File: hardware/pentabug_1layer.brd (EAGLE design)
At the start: 33 x 82.9 mm, 17 parts, among them IC1 ATMEGA88

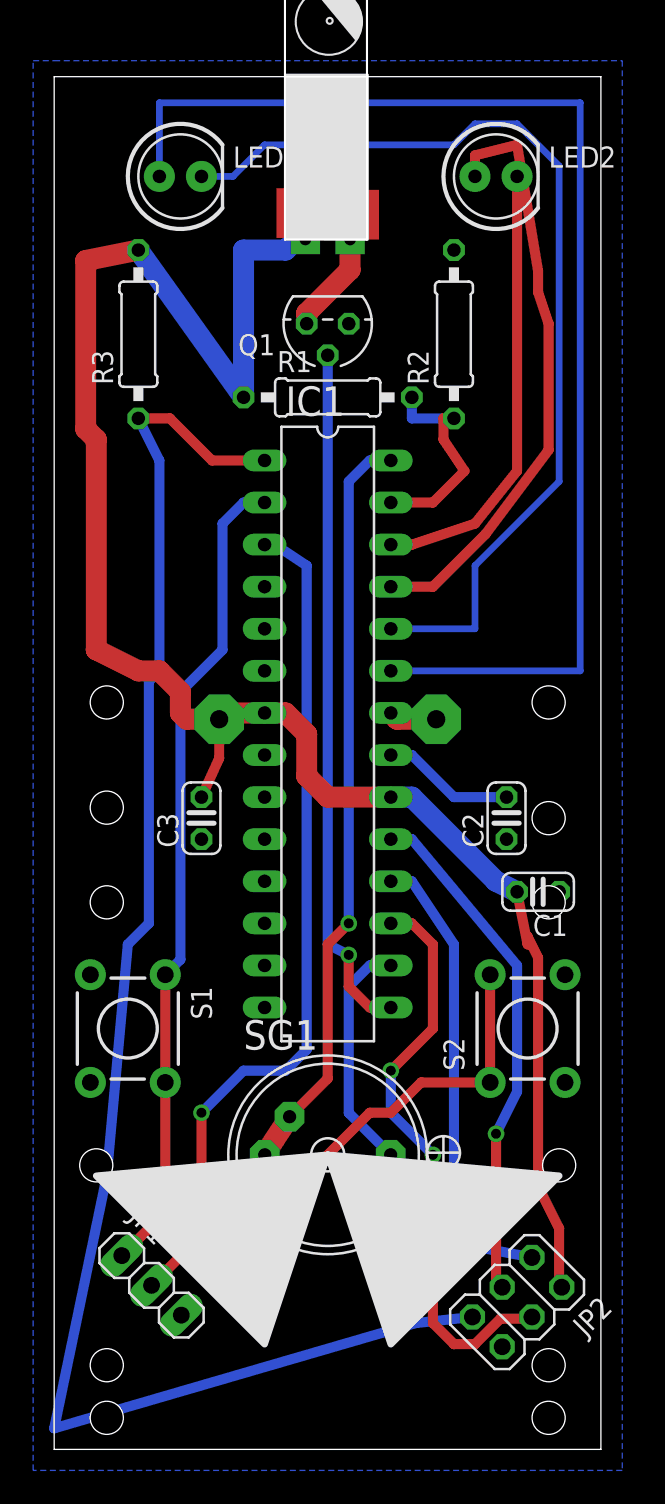
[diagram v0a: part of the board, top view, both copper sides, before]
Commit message: cleaned up and draw power lines
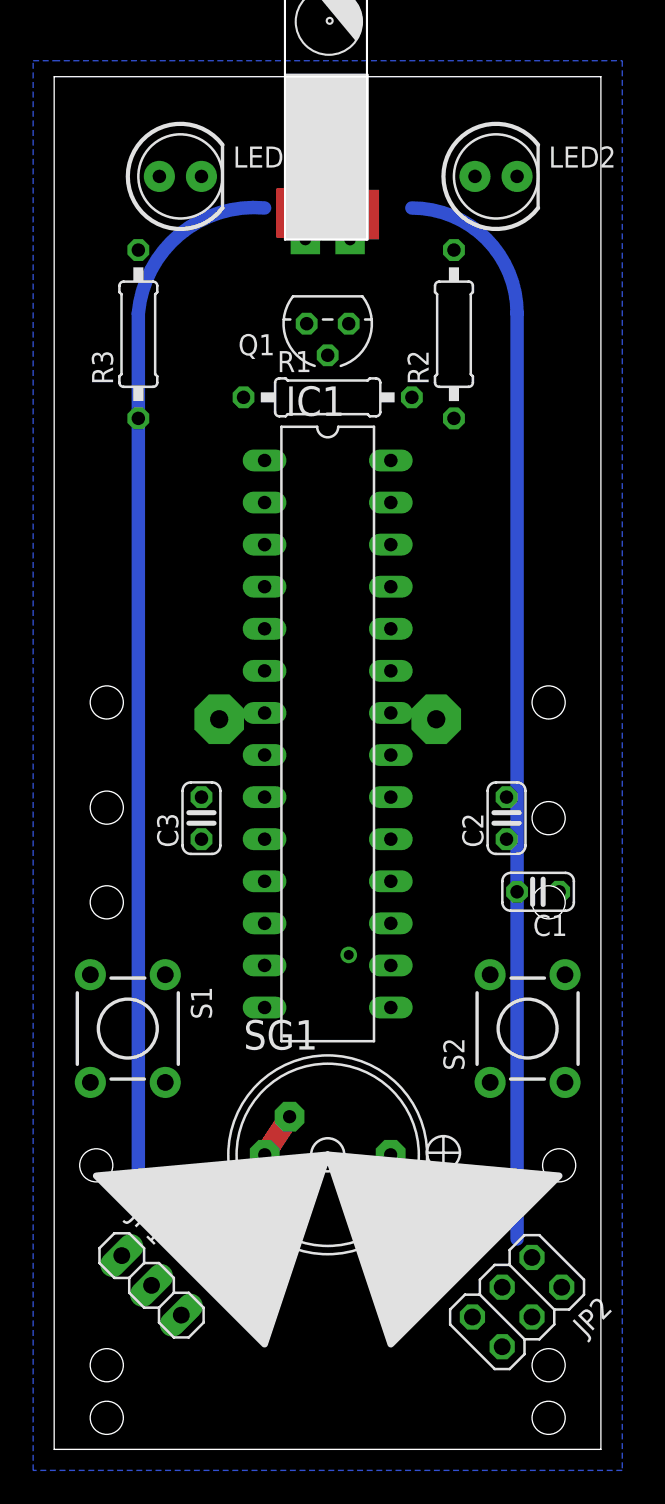
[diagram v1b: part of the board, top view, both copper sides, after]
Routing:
- net VCC: track 114.8 -> 0.00 mm
- net RST: track 97.3 -> 0.00 mm
- net TX: track 78.7 -> 0.00 mm, vias 1 -> 0
- net N$3: track 75.6 -> 0.00 mm
- net N$2: track 0.00 -> 64.9 mm
- net N$1: track 0.00 -> 63.3 mm
- net N$10: track 59.1 -> 0.00 mm
- net RX: track 49.8 -> 0.00 mm
- net BUZGND: track 42.9 -> 0.00 mm, vias 1 -> 0
- net VIBRATE: track 42.0 -> 0.00 mm
- net N$5: track 35.9 -> 0.00 mm
- net MOSI: track 35.2 -> 0.00 mm, vias 2 -> 0
- net SCK: track 31.1 -> 0.00 mm, vias 1 -> 0
- net MISO: track 28.6 -> 0.00 mm
- net BATTLVL: track 27.1 -> 0.00 mm
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
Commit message: made editable with eagle freeware!!
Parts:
- moved LED1 74.3 mm to (6.99, 8.89), turned to 90 degrees
- moved U$1 69.7 mm to (3.81, 17.8), turned to 180 degrees
- moved JP1 68.6 mm to (73.9, 7.15), turned to 45 degrees
- moved R3 68.3 mm to (16.5, 6.35), turned to 180 degrees
- moved S1 59.9 mm to (58.4, 5.71), turned to 0 degrees
- moved LED2 58.6 mm to (6.99, 27.9), turned to 90 degrees
- moved Q1 56.5 mm to (15.9, 17.8), turned to 270 degrees
- moved R1 52.2 mm to (20.3, 17.8), turned to 90 degrees
- moved C3 50.3 mm to (45.7, 10.2), turned to 180 degrees
- moved SG1 49.9 mm to (66.0, 17.8), turned to 90 degrees
- moved JP2 49.0 mm to (74.9, 29.2), turned to 315 degrees
- moved R2 48.9 mm to (16.5, 25.4), turned to 180 degrees
- moved BAT1 47.8 mm to (63.5, 17.8), turned to 180 degrees
- moved IC1 39.9 mm to (40.6, 17.8), turned to 0 degrees
- moved S2 29.9 mm to (58.4, 29.8), turned to 180 degrees
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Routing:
- net VCC: track 0.00 -> 137.0 mm
- net N$2: track 64.9 -> 0.00 mm
- net N$1: track 63.3 -> 0.00 mm
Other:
- board size 33 x 82.9 mm -> 82.9 x 33 mm

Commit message: inbetween
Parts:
- moved C1 5.08 mm to (50.2, 25.4)
- moved R3 3.59 mm to (19.1, 8.89)
- moved R2 2.84 mm to (19.1, 26.7)
- moved C2 2.01 mm to (45.1, 26.7)
- moved LED1 1.27 mm to (6.99, 7.62)
- moved C3 0.63 mm to (45.7, 9.53)
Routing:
- net RX: track 0.00 -> 48.5 mm
- net VCC: track 137.0 -> 184.7 mm
- net VIBRATE: track 0.00 -> 40.9 mm, vias 1 -> 0
- net TX: track 0.00 -> 38.7 mm, vias 0 -> 2
- net MOSI: track 0.00 -> 27.1 mm
- net MISO: track 0.00 -> 26.1 mm
- net RST: track 0.00 -> 23.9 mm
- net SCK: track 0.00 -> 17.5 mm
- net BATLVL: track 0.00 -> 13.9 mm
- net N$8: track 0.00 -> 5.97 mm
- net N$17: track 0.00 -> 5.72 mm
- net N$6: track 0.00 -> 0.64 mm

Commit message: inbetween
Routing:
- net BUZGND: track 0.00 -> 45.8 mm, vias 0 -> 2
- net TX: track 38.7 -> 71.9 mm, vias 2 -> 4
- net BUZZR: track 0.00 -> 13.0 mm
- net GND: track 0.00 -> 3.81 mm, vias 0 -> 2
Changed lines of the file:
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@@
 <grid distance="25" unitdist="mil" unit="mil" style="lines" multiple="2" display="yes" altdistance="10" altunitdist="mil" altunit="mil"/>
 <layers>
-<layer number="1" name="Top" color="4" fill="1" visible="no" active="yes"/>
+<layer number="1" name="Top" color="4" fill="1" visible="yes" active="yes"/>
 <layer number="2" name="Route2" color="1" fill="3" visible="no" active="no"/>
 <layer number="3" name="Route3" color="4" fill="3" visible="no" active="no"/>
@@
 <vertex x="85.09" y="0"/>
 </polygon>
-<wire x1="50.165" y1="26.67" x2="55.1688" y2="32.1056" width="0" layer="19" extent="1-1"/>
-<wire x1="41.91" y1="13.97" x2="39.37" y2="21.59" width="0" layer="19" extent="1-1"/>
+<via x="40.64" y="19.685" extent="1-16" drill="0.6" diameter="0.254" shape="octagon"/>
+<via x="40.64" y="15.875" extent="1-16" drill="0.6" diameter="0.254" shape="octagon"/>
+<wire x1="40.64" y1="19.685" x2="40.64" y2="15.875" width="0.4064" layer="1"/>
+<wire x1="46.355" y1="26.67" x2="39.75" y2="24.33" width="0" layer="19" extent="1-1"/>
+<wire x1="55.1688" y1="32.1056" x2="50.165" y2="26.67" width="0" layer="19" extent="1-1"/>
 <wire x1="55.1688" y1="3.4544" x2="46.99" y2="9.525" width="0" layer="19" extent="1-1"/>
+<wire x1="15.875" y1="19.05" x2="39.37" y2="21.59" width="0" layer="19" extent="1-1"/>
 </signal>
 <signal name="N$17">
@@
 <contactref element="JP1" pad="2"/>
 <contactref element="IC1" pad="3"/>
-<wire x1="60.96" y1="27.686" x2="55.88" y2="27.686" width="0.4064" layer="16"/>
+<wire x1="63.119" y1="27.686" x2="55.88" y2="27.686" width="0.4064" layer="16"/>
 <wire x1="55.626" y1="27.686" x2="33.401" y2="27.686" width="0.4064" layer="16"/>
 <wire x1="33.401" y1="27.686" x2="30.48" y2="24.765" width="0.4064" layer="16"/>
@@
 <wire x1="30.48" y1="15.748" x2="29.21" y2="13.97" width="0.4064" layer="16"/>
 <via x="30.48" y="19.685" extent="1-16" drill="0.6" diameter="0.254" shape="octagon"/>
-<wire x1="60.96" y1="27.686" x2="61.6712" y2="27.5844" width="0" layer="19" extent="16-16"/>
+<wire x1="30.48" y1="19.685" x2="30.48" y2="15.875" width="0.4064" layer="1"/>
+<via x="60.325" y="22.225" extent="1-16" drill="0.6" diameter="0.254" shape="octagon"/>
+<wire x1="60.325" y1="22.225" x2="73.914" y2="8.636" width="0.4064" layer="16"/>
+<wire x1="73.914" y1="8.636" x2="73.914" y2="7.112" width="0.4064" layer="16"/>
+<wire x1="63.5" y1="27.305" x2="60.325" y2="22.225" width="0.4064" layer="1"/>
+<wire x1="63.119" y1="27.686" x2="63.5" y2="27.305" width="0.4064" layer="16"/>
+<via x="63.5" y="27.432" extent="1-16" drill="0.6" diameter="0.254" shape="octagon"/>
+<wire x1="63.5" y1="27.305" x2="63.5" y2="27.432" width="0" layer="19" extent="16-16"/>
+<wire x1="63.5" y1="27.305" x2="63.5" y2="27.305" width="0" layer="19" extent="1-16"/>
+<wire x1="73.92" y1="7.147" x2="73.914" y2="7.112" width="0" layer="19" extent="16-16"/>
 <wire x1="55.626" y1="27.686" x2="55.88" y2="27.686" width="0" layer="19" extent="16-16"/>
+<wire x1="30.48" y1="15.748" x2="30.48" y2="15.875" width="0" layer="19" extent="1-1"/>
 <wire x1="55.1688" y1="27.5844" x2="55.626" y2="27.686" width="0" layer="19" extent="16-16"/>
-<wire x1="30.48" y1="15.748" x2="30.48" y2="19.685" width="0" layer="19" extent="16-16"/>
-<wire x1="73.92" y1="7.147" x2="61.6712" y2="27.5844" width="0" layer="19" extent="1-1"/>
+<wire x1="61.6712" y1="27.5844" x2="63.119" y2="27.686" width="0" layer="19" extent="16-16"/>
 </signal>
 <signal name="RX">
@@
 <contactref element="SG1" pad="+1"/>
 <contactref element="SG1" pad="+"/>
+<wire x1="66.04" y1="21.59" x2="64.135" y2="23.495" width="0.4064" layer="16"/>
+<wire x1="64.135" y1="23.495" x2="56.515" y2="23.495" width="0.4064" layer="16"/>
+<wire x1="56.515" y1="23.495" x2="54.61" y2="21.59" width="0.4064" layer="16"/>
 <wire x1="66.04" y1="21.59" x2="66.04" y2="21.58" width="0" layer="19" extent="1-1"/>
-<wire x1="54.61" y1="21.59" x2="66.04" y2="21.58" width="0" layer="19" extent="1-1"/>
+<wire x1="66.04" y1="21.59" x2="66.04" y2="21.59" width="0" layer="19" extent="1-16"/>
 </signal>
 <signal name="VIBRATE">
@@
 <contactref element="SG1" pad="-1"/>
 <contactref element="SG1" pad="-"/>
+<wire x1="63.754" y1="15.494" x2="63.373" y2="15.875" width="0.4064" layer="16"/>
+<wire x1="63.373" y1="15.875" x2="42.545" y2="15.875" width="0.4064" layer="16"/>
+<via x="42.545" y="15.875" extent="1-16" drill="0.6" diameter="0.254" shape="octagon"/>
+<wire x1="24.13" y1="21.59" x2="27.305" y2="18.415" width="0.4064" layer="16"/>
+<wire x1="27.305" y1="18.415" x2="41.91" y2="18.415" width="0.4064" layer="16"/>
+<via x="42.545" y="19.685" extent="1-16" drill="0.6" diameter="0.254" shape="octagon"/>
+<wire x1="41.91" y1="18.415" x2="42.545" y2="19.05" width="0.4064" layer="16"/>
+<wire x1="42.545" y1="19.05" x2="42.545" y2="19.685" width="0.4064" layer="16"/>
+<wire x1="42.545" y1="19.685" x2="42.545" y2="15.875" width="0.4064" layer="1"/>
 <wire x1="66.04" y1="13.98" x2="66.04" y2="13.97" width="0" layer="19" extent="1-1"/>
-<wire x1="24.13" y1="21.59" x2="63.74" y2="15.48" width="0" layer="19" extent="1-1"/>
+<wire x1="63.754" y1="15.494" x2="63.74" y2="15.48" width="0" layer="19" extent="16-16"/>
 </signal>
 <signal name="PD7">

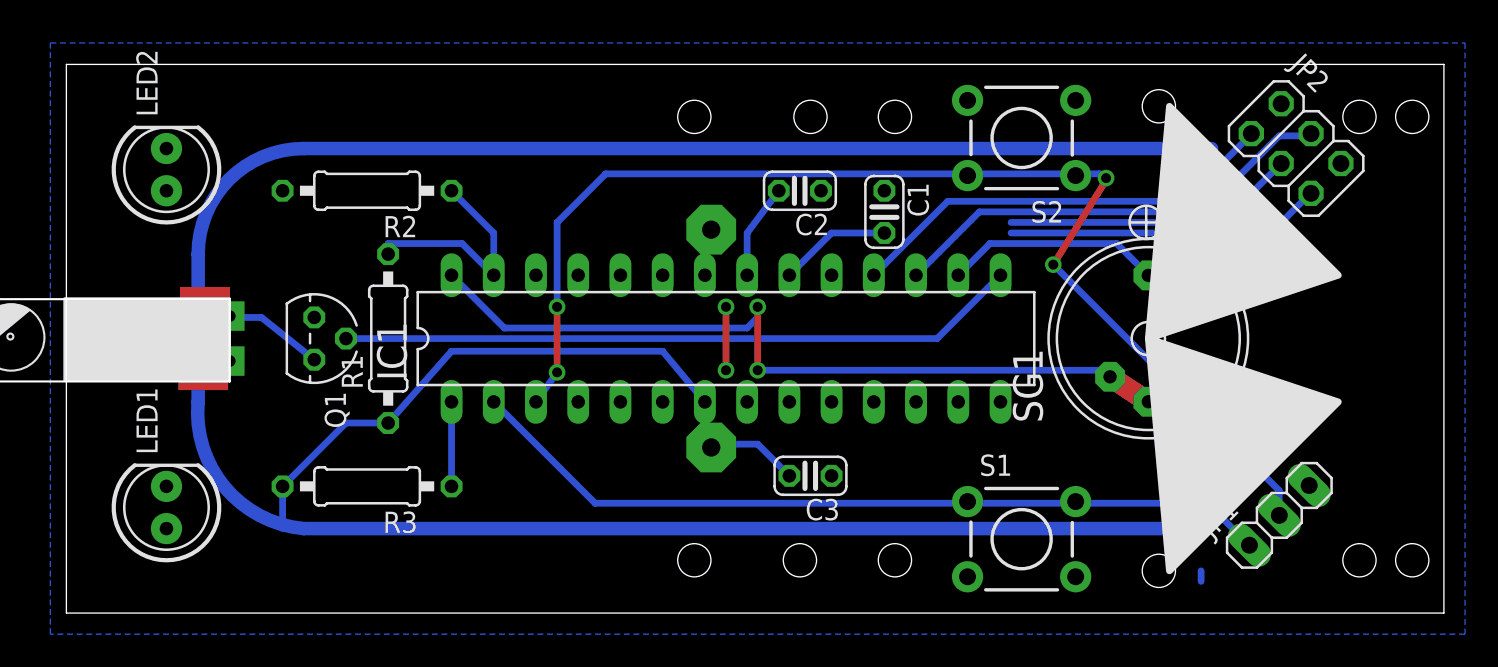
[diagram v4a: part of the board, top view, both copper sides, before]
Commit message: close to final - mass remaining
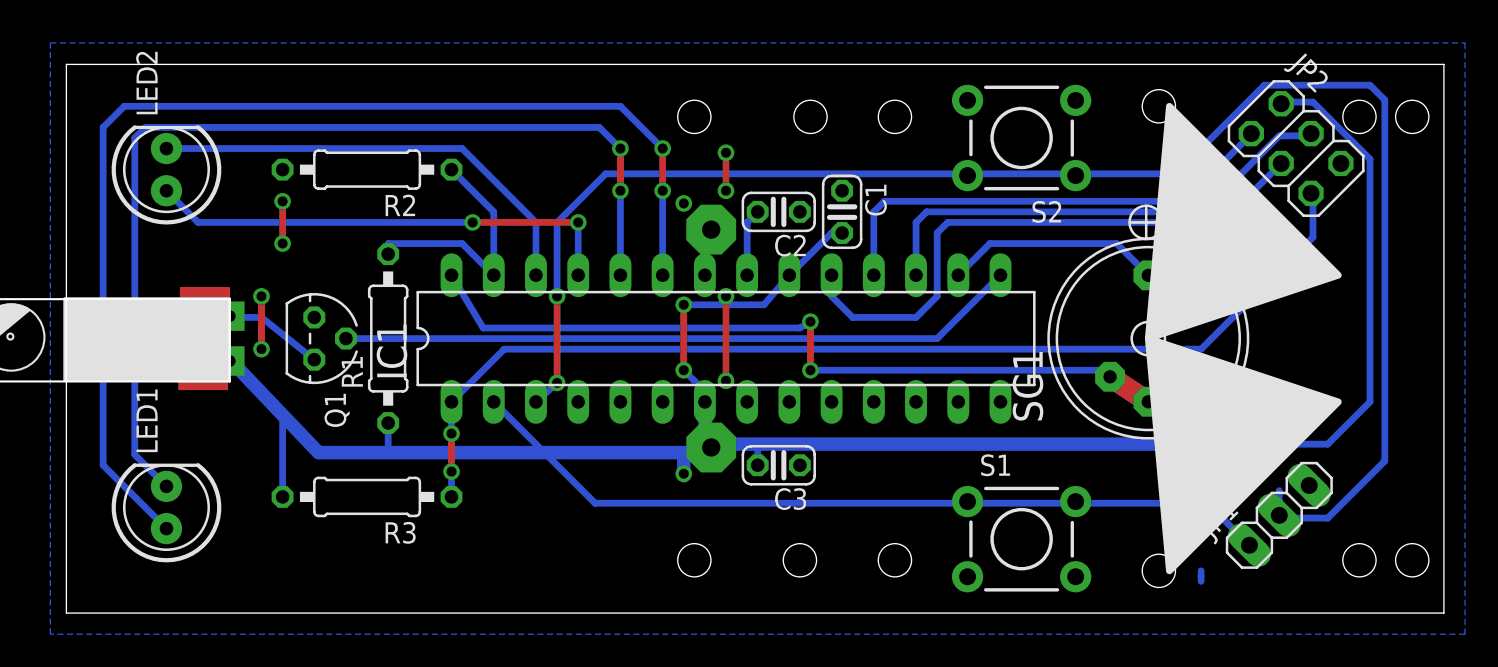
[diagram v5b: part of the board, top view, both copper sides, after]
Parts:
- moved C1 2.54 mm to (47.6, 25.4)
- moved C3 2.01 mm to (43.8, 10.2)
- moved C2 1.80 mm to (43.8, 25.4)
- moved R2 1.27 mm to (19.1, 27.9)
- moved R3 0.63 mm to (19.1, 8.26)
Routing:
- net N$3: track 0.00 -> 68.6 mm, vias 0 -> 2
- net N$10: track 0.00 -> 59.4 mm, vias 0 -> 2
- net VCC: track 184.7 -> 125.4 mm, vias 0 -> 2
- net RST: track 23.9 -> 64.0 mm, vias 0 -> 2
- net N$5: track 0.00 -> 28.7 mm, vias 0 -> 2
- net BATTLVL: track 0.00 -> 27.2 mm
- net TX: track 71.9 -> 95.4 mm, vias 4 -> 2
- net SCK: track 17.5 -> 34.7 mm
- net GND: track 3.81 -> 13.1 mm, vias 2 -> 8
- net MISO: track 26.1 -> 28.3 mm
- net MOSI: track 27.1 -> 29.0 mm
- net N$17: track 5.72 -> 4.07 mm
- net N$23: track 0.00 -> 1.27 mm
- net BATLVL: track 13.9 -> 15.2 mm
- net BUZGND: track 45.8 -> 44.6 mm

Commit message: inbetween
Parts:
- turned LED2 to 270 degrees
- turned S2 to 0 degrees
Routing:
- net TX: track 95.4 -> 108.1 mm
- net GND: track 13.1 -> 3.18 mm, vias 8 -> 2
- net RX: track 48.5 -> 51.1 mm, vias 0 -> 2
- net N$5: track 28.7 -> 29.8 mm, vias 2 -> 0
- net BATTLVL: track 27.2 -> 28.1 mm
- net N$6: track 0.64 -> 0.00 mm
- net N$10: vias 2 -> 0
- net N$3: vias 2 -> 0

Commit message: final 0.1
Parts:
- moved C3 1.02 mm to (43.8, 9.14)
- turned S1 to 180 degrees
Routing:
- net GND: track 3.18 -> 47.6 mm, vias 2 -> 20
- net VCC: track 125.4 -> 140.9 mm, vias 2 -> 0
- net BUZGND: track 44.6 -> 47.4 mm
- net BUZZR: track 13.0 -> 15.3 mm
- net RX: track 51.1 -> 53.3 mm
- net N$24: track 5.97 -> 7.03 mm
- net TX: track 108.1 -> 108.6 mm

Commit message: some synth --- sync
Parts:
- moved SG1 2.54 mm to (68.6, 17.8)
- moved S1 1.27 mm to (58.4, 6.99)
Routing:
- net VCC: track 140.9 -> 162.6 mm, vias 0 -> 2
- net BUZZR: track 15.3 -> 0.00 mm
- net RST: track 64.0 -> 75.5 mm, vias 2 -> 0
- net RX: track 53.3 -> 47.1 mm, vias 2 -> 0
- net GND: track 47.6 -> 43.3 mm, vias 20 -> 16
- net BUZGND: track 47.4 -> 43.7 mm, vias 2 -> 0
- net SCK: track 34.7 -> 37.4 mm
- net VIBRATE: track 40.9 -> 43.2 mm
- net N$8: track 7.03 -> 7.90 mm
- net TX: track 108.6 -> 107.8 mm, vias 2 -> 0
